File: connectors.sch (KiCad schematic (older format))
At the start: 4 parts

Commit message: Arranged symbols
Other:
- moved on the sheet: J?
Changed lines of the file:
@@
 L Connector_Generic:Conn_01x04 J?
 U 1 1 5E9B3DBD
-P 6250 3350
-F 0 "J?" H 6330 3342 50  0000 L CNN
-F 1 "Conn_01x04" H 6330 3251 50  0000 L CNN
-F 2 "" H 6250 3350 50  0001 C CNN
-F 3 "~" H 6250 3350 50  0001 C CNN
-	1    6250 3350
+P 4900 2350
+F 0 "J?" H 4980 2342 50  0000 L CNN
+F 1 "Conn_01x04" H 4980 2251 50  0000 L CNN
+F 2 "" H 4900 2350 50  0001 C CNN
+F 3 "~" H 4900 2350 50  0001 C CNN
+	1    4900 2350
 	1    0    0    -1
 $EndComp
@@
 L Connector_Generic:Conn_02x03_Odd_Even J?
 U 1 1 5E9B44E9
-P 6000 4350
-F 0 "J?" H 6050 4667 50  0000 C CNN
-F 1 "Conn_02x03_Odd_Even" H 6050 4576 50  0000 C CNN
-F 2 "" H 6000 4350 50  0001 C CNN
-F 3 "~" H 6000 4350 50  0001 C CNN
-	1    6000 4350
+P 6350 3500
+F 0 "J?" H 6400 3817 50  0000 C CNN
+F 1 "Conn_02x03_Odd_Even" H 6400 3726 50  0000 C CNN
+F 2 "" H 6350 3500 50  0001 C CNN
+F 3 "~" H 6350 3500 50  0001 C CNN
+	1    6350 3500
 	1    0    0    -1
 $EndComp
@@
 L Connector_Generic:Conn_01x04 J?
 U 1 1 5E9B4FBB
-P 7200 4300
-F 0 "J?" H 7280 4292 50  0000 L CNN
-F 1 "Conn_01x04" H 7280 4201 50  0000 L CNN
-F 2 "" H 7200 4300 50  0001 C CNN
-F 3 "~" H 7200 4300 50  0001 C CNN
-	1    7200 4300
+P 6350 2300
+F 0 "J?" H 6430 2292 50  0000 L CNN
+F 1 "Conn_01x04" H 6430 2201 50  0000 L CNN
+F 2 "" H 6350 2300 50  0001 C CNN
+F 3 "~" H 6350 2300 50  0001 C CNN
+	1    6350 2300
 	1    0    0    -1
 $EndComp

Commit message: Annotated
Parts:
- gave numbers to parts that had none: 4
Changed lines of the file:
@@
 $EndDescr
 $Comp
-L Connector_Generic:Conn_01x09 J?
+L Connector_Generic:Conn_01x09 J2
 U 1 1 5E9B3209
 P 4900 3450
-F 0 "J?" H 4980 3492 50  0000 L CNN
+F 0 "J2" H 4980 3492 50  0000 L CNN
 F 1 "Conn_01x09" H 4980 3401 50  0000 L CNN
 F 2 "" H 4900 3450 50  0001 C CNN
@@
 $EndComp
 $Comp
-L Connector_Generic:Conn_01x04 J?
+L Connector_Generic:Conn_01x04 J1
 U 1 1 5E9B3DBD
 P 4900 2350
-F 0 "J?" H 4980 2342 50  0000 L CNN
+F 0 "J1" H 4980 2342 50  0000 L CNN
 F 1 "Conn_01x04" H 4980 2251 50  0000 L CNN
 F 2 "" H 4900 2350 50  0001 C CNN
@@
 $EndComp
 $Comp
-L Connector_Generic:Conn_02x03_Odd_Even J?
+L Connector_Generic:Conn_02x03_Odd_Even J4
 U 1 1 5E9B44E9
 P 6350 3500
-F 0 "J?" H 6400 3817 50  0000 C CNN
+F 0 "J4" H 6400 3817 50  0000 C CNN
 F 1 "Conn_02x03_Odd_Even" H 6400 3726 50  0000 C CNN
 F 2 "" H 6350 3500 50  0001 C CNN
@@
 $EndComp
 $Comp
-L Connector_Generic:Conn_01x04 J?
+L Connector_Generic:Conn_01x04 J3
 U 1 1 5E9B4FBB
 P 6350 2300
-F 0 "J?" H 6430 2292 50  0000 L CNN
+F 0 "J3" H 6430 2292 50  0000 L CNN
 F 1 "Conn_01x04" H 6430 2201 50  0000 L CNN
 F 2 "" H 6350 2300 50  0001 C CNN

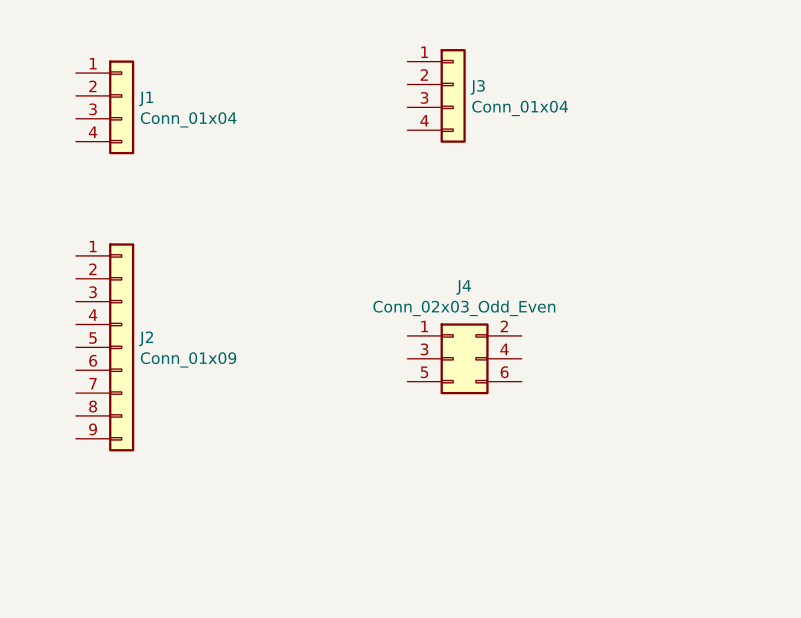
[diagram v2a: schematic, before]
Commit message: added components lables and footprints
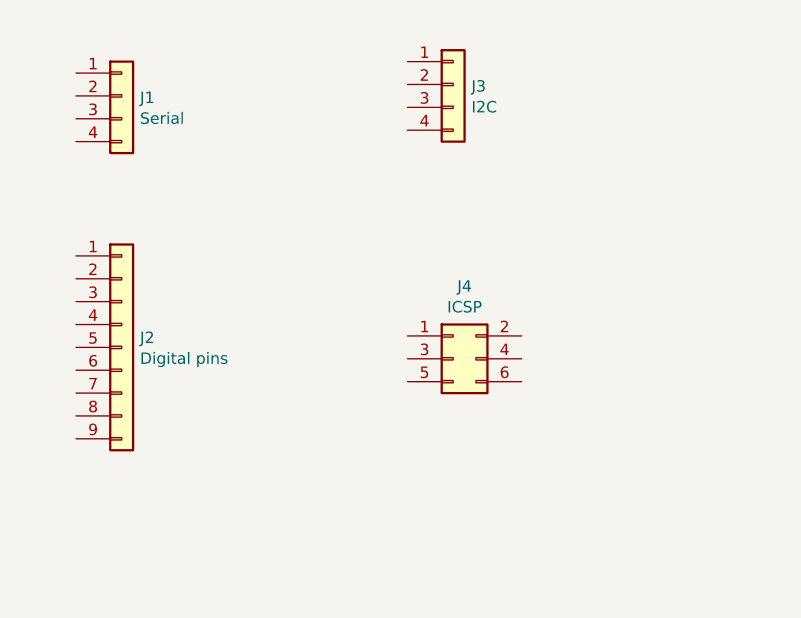
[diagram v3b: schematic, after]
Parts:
- J1: value Conn_01x04 -> Serial; footprint (none) -> Connector_PinSocket_2.54mm:PinSocket_1x04_P2.54mm_Vertical
- J2: value Conn_01x09 -> Digital pins; footprint (none) -> Connector_PinSocket_2.54mm:PinSocket_1x09_P2.54mm_Vertical
- J3: value Conn_01x04 -> I2C; footprint (none) -> Connector_PinSocket_2.54mm:PinSocket_1x04_P2.54mm_Vertical
- J4: value Conn_02x03_Odd_Even -> ICSP; footprint (none) -> Connector_PinSocket_2.54mm:PinSocket_2x03_P2.54mm_Vertical
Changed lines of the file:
@@
 P 4900 3450
 F 0 "J2" H 4980 3492 50  0000 L CNN
-F 1 "Conn_01x09" H 4980 3401 50  0000 L CNN
-F 2 "" H 4900 3450 50  0001 C CNN
+F 1 "Digital pins" H 4980 3401 50  0000 L CNN
+F 2 "Connector_PinSocket_2.54mm:PinSocket_1x09_P2.54mm_Vertical" H 4900 3450 50  0001 C CNN
 F 3 "~" H 4900 3450 50  0001 C CNN
 	1    4900 3450
@@
 P 4900 2350
 F 0 "J1" H 4980 2342 50  0000 L CNN
-F 1 "Conn_01x04" H 4980 2251 50  0000 L CNN
-F 2 "" H 4900 2350 50  0001 C CNN
+F 1 "Serial" H 4980 2251 50  0000 L CNN
+F 2 "Connector_PinSocket_2.54mm:PinSocket_1x04_P2.54mm_Vertical" H 4900 2350 50  0001 C CNN
 F 3 "~" H 4900 2350 50  0001 C CNN
 	1    4900 2350
@@
 P 6350 3500
 F 0 "J4" H 6400 3817 50  0000 C CNN
-F 1 "Conn_02x03_Odd_Even" H 6400 3726 50  0000 C CNN
-F 2 "" H 6350 3500 50  0001 C CNN
+F 1 "ICSP" H 6400 3726 50  0000 C CNN
+F 2 "Connector_PinSocket_2.54mm:PinSocket_2x03_P2.54mm_Vertical" H 6350 3500 50  0001 C CNN
 F 3 "~" H 6350 3500 50  0001 C CNN
 	1    6350 3500
@@
 P 6350 2300
 F 0 "J3" H 6430 2292 50  0000 L CNN
-F 1 "Conn_01x04" H 6430 2201 50  0000 L CNN
-F 2 "" H 6350 2300 50  0001 C CNN
+F 1 "I2C" H 6430 2201 50  0000 L CNN
+F 2 "Connector_PinSocket_2.54mm:PinSocket_1x04_P2.54mm_Vertical" H 6350 2300 50  0001 C CNN
 F 3 "~" H 6350 2300 50  0001 C CNN
 	1    6350 2300

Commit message: Completed wiring in the connectors sheet
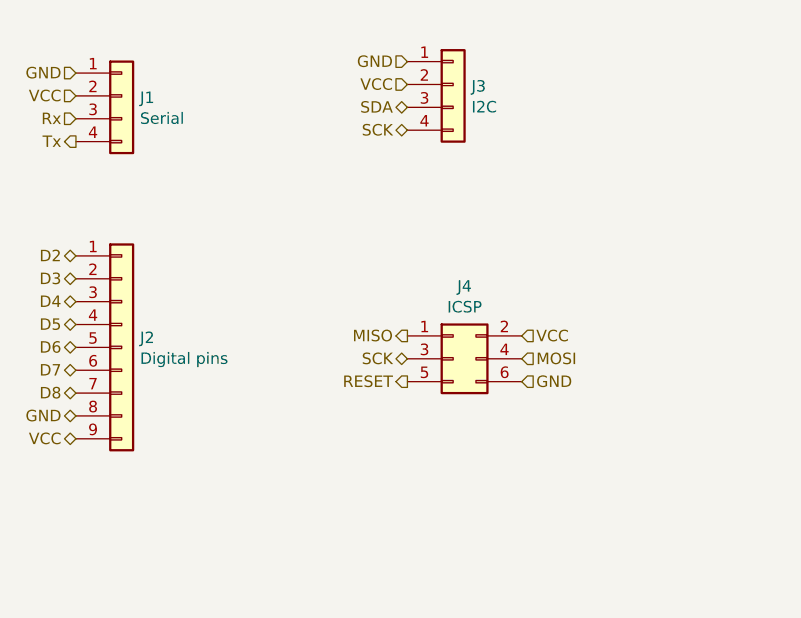
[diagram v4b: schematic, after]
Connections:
- net D2: now reaches J2.1 (Pin_1)
- net D3: now reaches J2.2 (Pin_2)
- net D4: now reaches J2.3 (Pin_3)
- net D5: now reaches J2.4 (Pin_4)
- net D6: now reaches J2.5 (Pin_5)
- net D7: now reaches J2.6 (Pin_6)
- net D8: now reaches J2.7 (Pin_7)
- net GND: now reaches J2.8 (Pin_8)
- net GND: now also J1.1 (Pin_1), J3.1 (Pin_1), J4.6 (Pin_6)
- net VCC: now reaches J2.9 (Pin_9)
- net VCC: now also J1.2 (Pin_2), J3.2 (Pin_2), J4.2 (Pin_2)
- net Rx: now reaches J1.3 (Pin_3)
- net Tx: now reaches J1.4 (Pin_4)
- net MISO: now reaches J4.1 (Pin_1)
- net SCK: now reaches J4.3 (Pin_3)
- net SCK: now also J3.4 (Pin_4)
- net MOSI: now reaches J4.4 (Pin_4)
- net RESET: now reaches J4.5 (Pin_5)
- net SDA: now reaches J3.3 (Pin_3)
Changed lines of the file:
@@
 	1    0    0    -1
 $EndComp
+Text HLabel 6150 3400 0    50   Output ~ 0
+MISO
+Text HLabel 6150 3500 0    50   BiDi ~ 0
+SCK
+Text HLabel 6150 3600 0    50   Output ~ 0
+RESET
+Text HLabel 6650 3400 2    50   Input ~ 0
+VCC
+Text HLabel 6650 3500 2    50   Input ~ 0
+MOSI
+Text HLabel 6650 3600 2    50   Input ~ 0
+GND
+Text HLabel 4700 2250 0    50   Input ~ 0
+GND
+Text HLabel 4700 2350 0    50   Input ~ 0
+VCC
+Text HLabel 4700 2450 0    50   Input ~ 0
+Rx
+Text HLabel 4700 2550 0    50   Output ~ 0
+Tx
+Text HLabel 6150 2200 0    50   Input ~ 0
+GND
+Text HLabel 6150 2300 0    50   Input ~ 0
+VCC
+Text HLabel 6150 2400 0    50   BiDi ~ 0
+SDA
+Text HLabel 6150 2500 0    50   BiDi ~ 0
+SCK
+Text HLabel 4700 3050 0    50   BiDi ~ 0
+D2
+Text HLabel 4700 3150 0    50   BiDi ~ 0
+D3
+Text HLabel 4700 3250 0    50   BiDi ~ 0
+D4
+Text HLabel 4700 3350 0    50   BiDi ~ 0
+D5
+Text HLabel 4700 3450 0    50   BiDi ~ 0
+D6
+Text HLabel 4700 3550 0    50   BiDi ~ 0
+D7
+Text HLabel 4700 3650 0    50   BiDi ~ 0
+D8
+Text HLabel 4700 3850 0    50   BiDi ~ 0
+VCC
+Text HLabel 4700 3750 0    50   BiDi ~ 0
+GND
 $EndSCHEMATC

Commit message: created netlist file
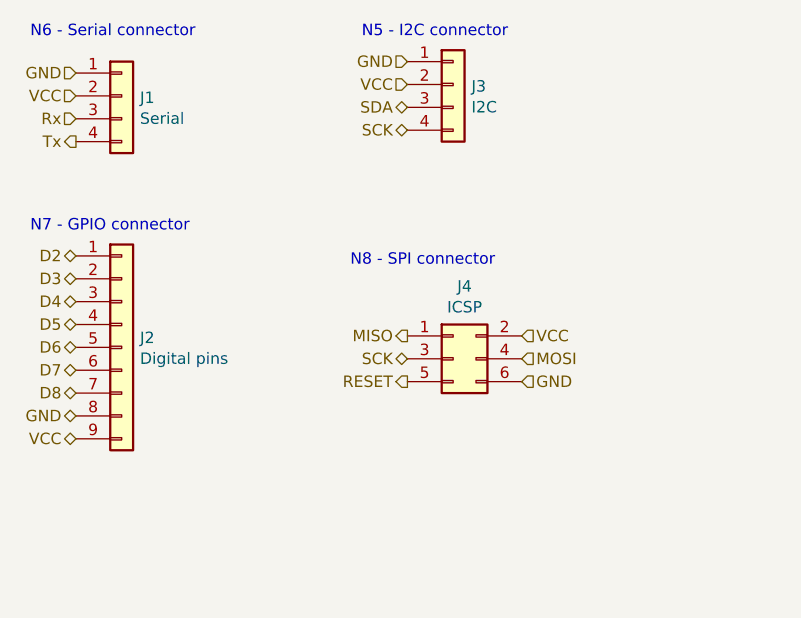
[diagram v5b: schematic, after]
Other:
- note added: "N5 - I2C connector"
- note added: "N6 - Serial connector"
- note added: "N7 - GPIO connector"
- note added: "N8 - SPI connector"
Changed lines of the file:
@@
 Text HLabel 4700 3750 0    50   BiDi ~ 0
 GND
+Text Notes 4500 2100 0    50   ~ 0
+N6 - Serial connector
+Text Notes 5950 2100 0    50   ~ 0
+N5 - I2C connector
+Text Notes 4500 2950 0    50   ~ 0
+N7 - GPIO connector
+Text Notes 5900 3100 0    50   ~ 0
+N8 - SPI connector
 $EndSCHEMATC
